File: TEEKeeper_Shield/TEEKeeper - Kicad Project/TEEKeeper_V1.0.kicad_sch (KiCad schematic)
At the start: 26 parts, among them J1 GX16-4, J10 Screw_Terminal_01x03, J11 Screw_Terminal_01x01, J2 GX20-3, J3 Screw_Terminal_01x04, J4 Screw_Terminal_01x04, J5 GX16-4, J9 Screw_Terminal_01x03, K1 Master relay

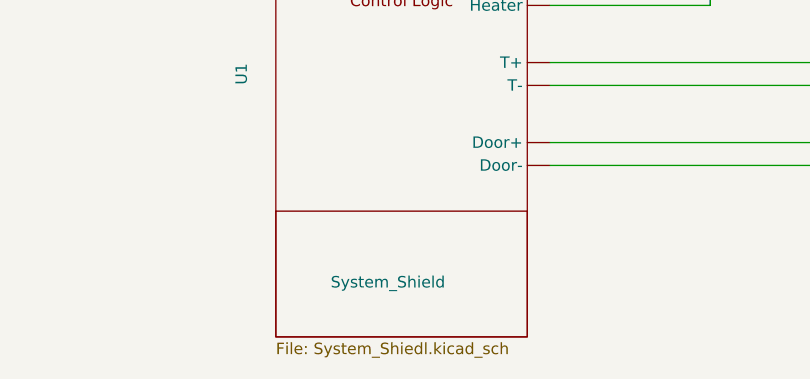
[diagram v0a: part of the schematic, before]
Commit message: Resolved minor issues
Fixed broken / bad designed reference connections, fixed pcb courtyard and edges, general cleanup
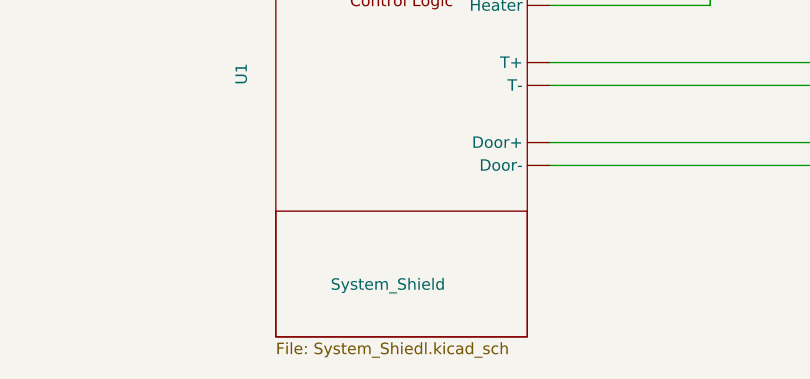
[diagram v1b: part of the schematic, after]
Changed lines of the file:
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@@
 		)
 		(property "Sheetname" "System_Shield"
-			(at 87.376 167.386 0)
+			(at 87.376 167.64 0)
 			(effects
 				(font

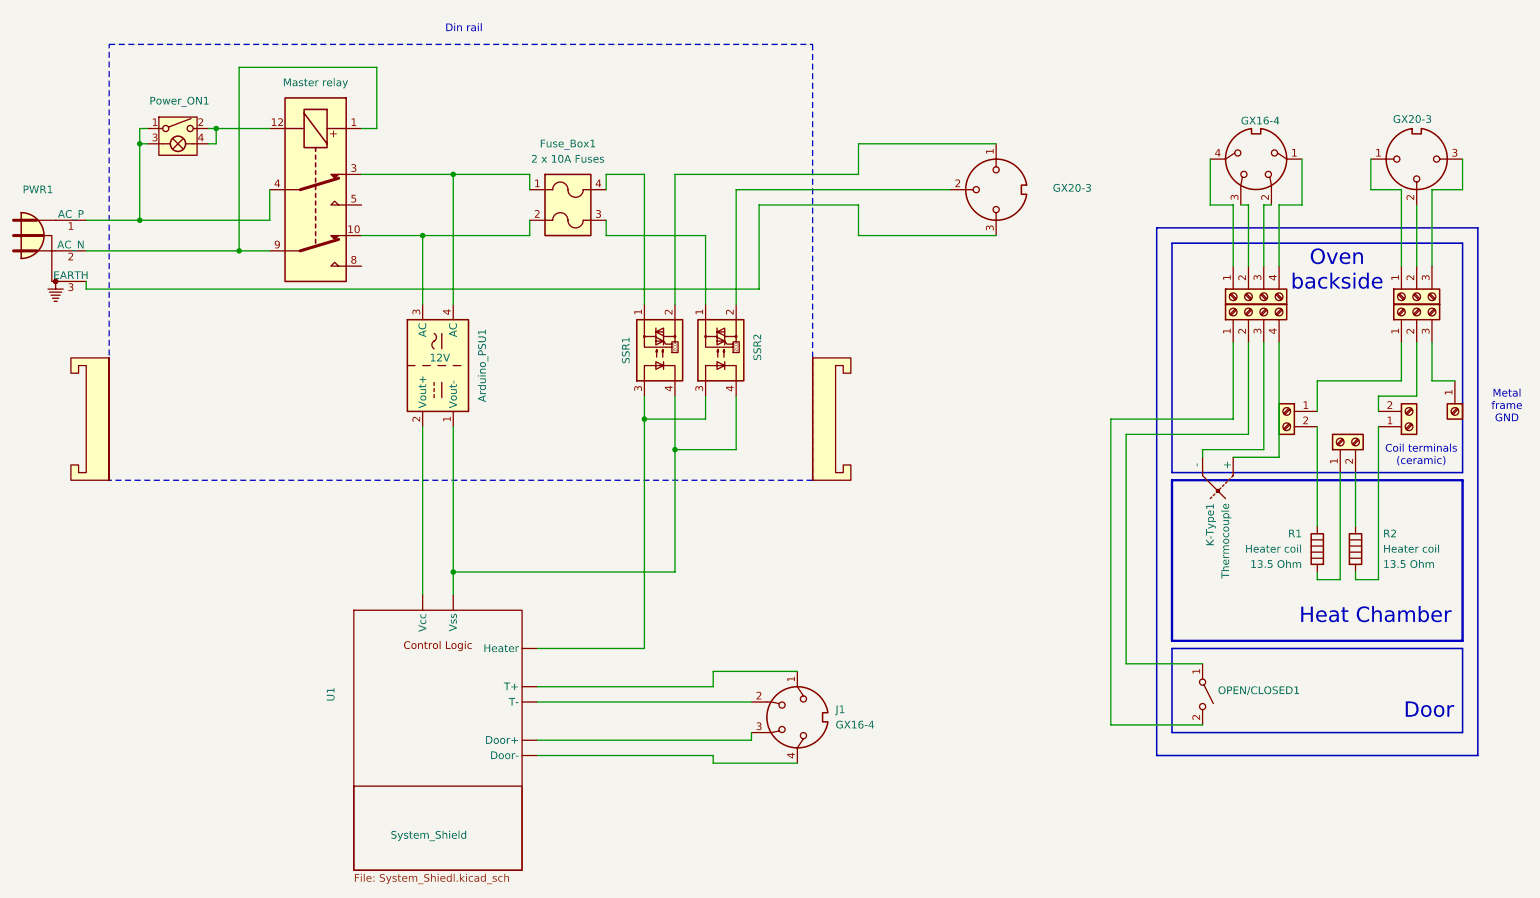
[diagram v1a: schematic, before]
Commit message: updated schematics
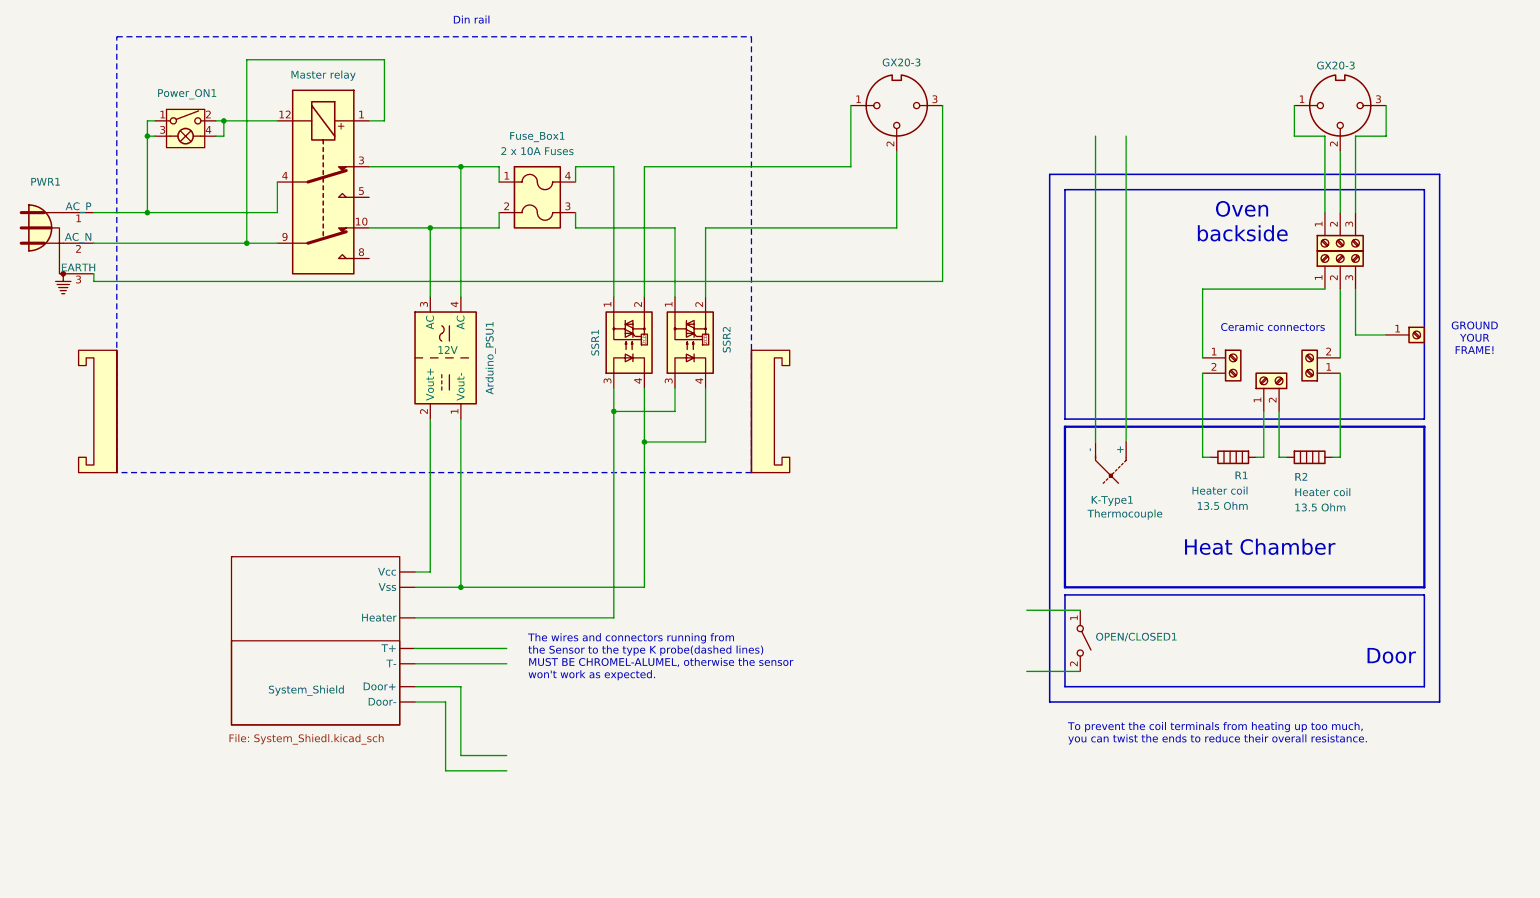
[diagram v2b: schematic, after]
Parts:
- removed J1, J5: GX16-4, symbol Connector:DIN-4
- removed J3, J4: Screw_Terminal_01x04, symbol Connector:Screw_Terminal_01x04
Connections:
- net at J8.1 (Pin_1): now also R2.1; no longer R2.2
- net at J7.2 (Pin_2): now also R2.2; no longer R2.1
- now unconnected: U1. (Vss), U1. (Vss), U1. (Vss)
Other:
- note added: "Ceramic connectors"
- note added: "GROUND YOUR FRAME!"
- note added: "The wires and connectors running from the Sensor to the type K probe(dashed lines) MUST BE CHROMEL-ALUMEL, otherwise the sensor won't work as expected."
- note added: "To prevent the coil terminals from heating up too much, you can twist the ends to reduce their overall resistance."
- note removed: "Coil terminals (ceramic)"
- note removed: "Metal frame GND"
- moved on the sheet: Arduino_PSU1, Fuse_Box1, K-Type1, OPEN/CLOSED1, PWR1, Power_ON1, R1, R2, SSR1, SSR2
